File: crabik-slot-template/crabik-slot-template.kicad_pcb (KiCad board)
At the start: 2 copper layers, 50.8 x 50.8 mm, 49 parts, among them J1 Battery, J1 UP (A), J15 CENTER (C) (1), J16 CENTER (D) (1), J17 CENTER (C) (2), J18 CENTER (D) (2), J19 CENTER (C) (3), J2 DOWN (A), J2 QWIIC, J20 CENTER (D) (3), J4 UP (B), J5 DOWN (B), P1 USB-C, SW1 Reset button

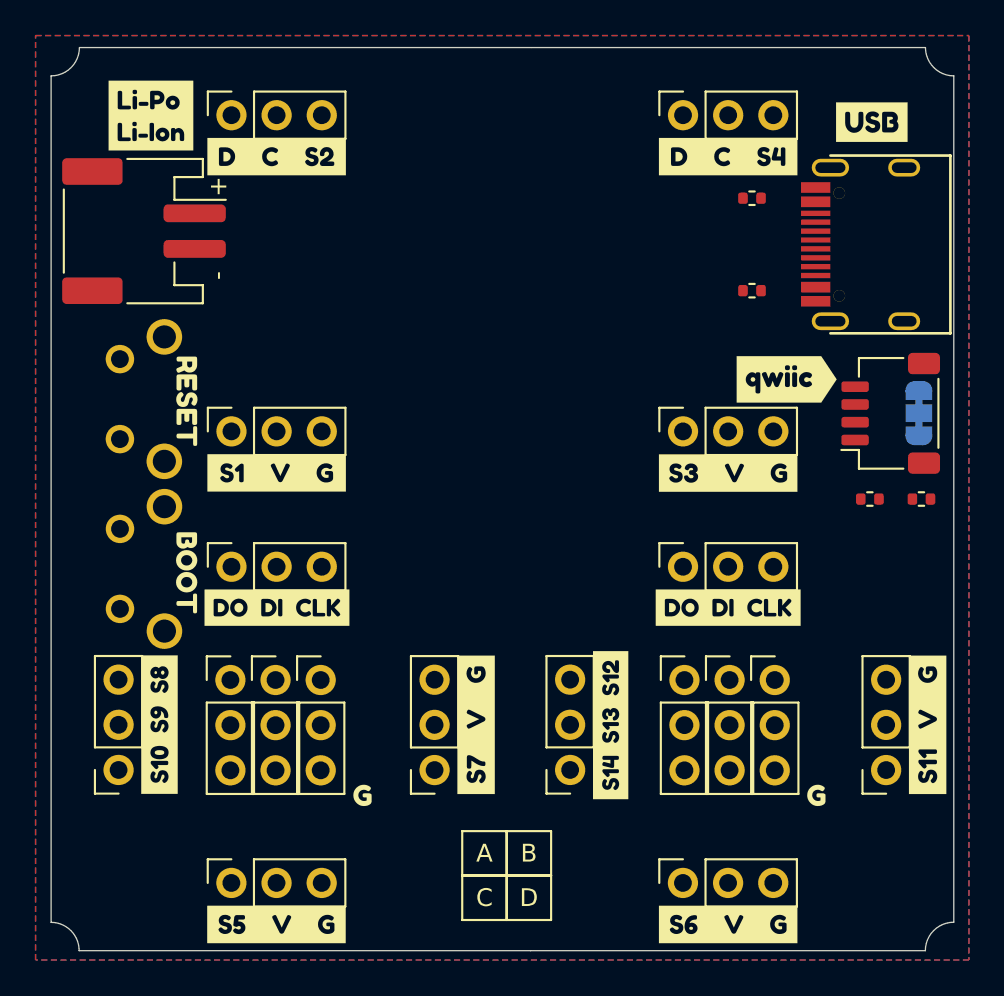
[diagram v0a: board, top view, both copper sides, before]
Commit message: Update templates and CI
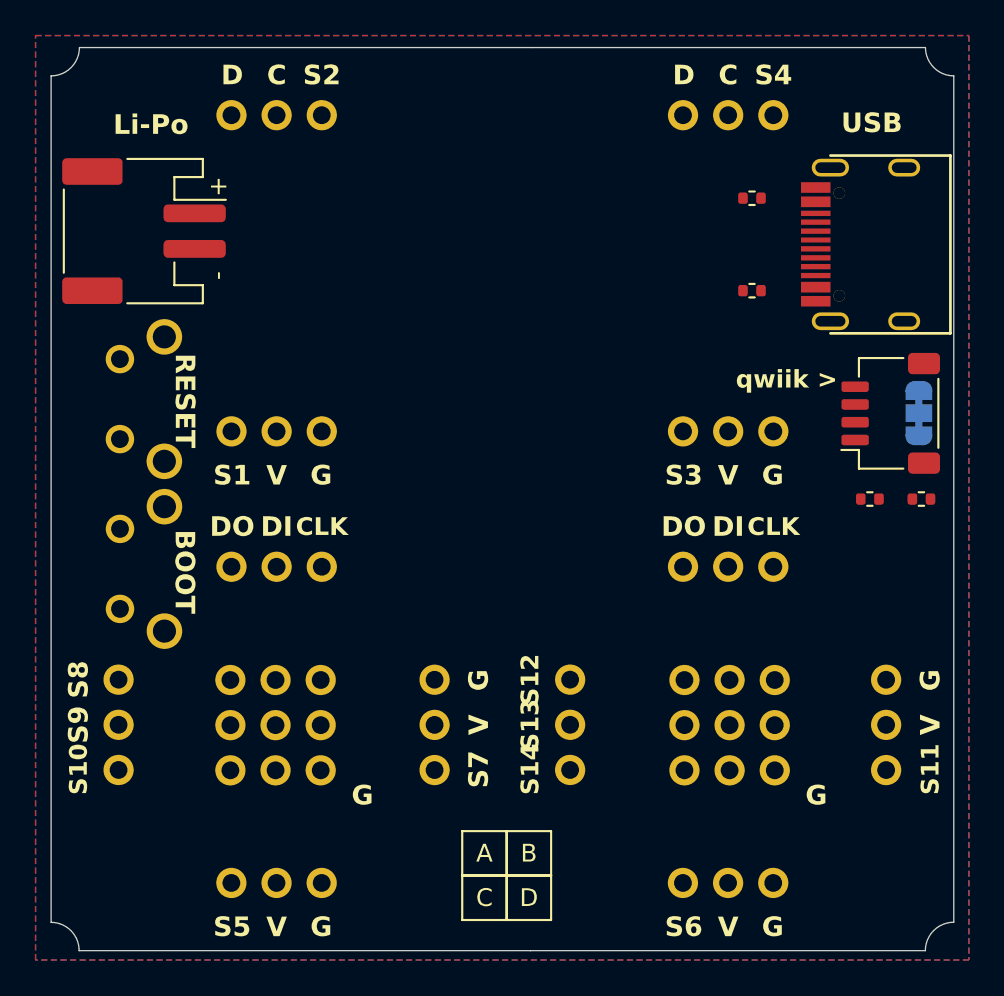
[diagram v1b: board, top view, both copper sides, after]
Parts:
- removed kibuzzard-637F66BD: G***, kibuzzard-637F66BD
- removed kibuzzard-637F7041: G***, kibuzzard-637F7041
- removed kibuzzard-637F708F: G***, kibuzzard-637F708F
- removed kibuzzard-63C28786: G***, kibuzzard-63C28786
- removed kibuzzard-63C28790: G***, kibuzzard-63C28790
- removed kibuzzard-63CA6CBF: G***, kibuzzard-63CA6CBF
- removed kibuzzard-63CE9BA7: G***, kibuzzard-63CE9BA7
- removed kibuzzard-63CFAB43: G***, kibuzzard-63CFAB43
- removed kibuzzard-63CFAB7C: G***, kibuzzard-63CFAB7C
- removed kibuzzard-63CFACF8: G***, kibuzzard-63CFACF8
- removed kibuzzard-63CFADAC: G***, kibuzzard-63CFADAC
- removed kibuzzard-63CFAED5: G***, kibuzzard-63CFAED5
- removed kibuzzard-63CFAF5C: G***, kibuzzard-63CFAF5C
- removed kibuzzard-63CFAFAA: G***, kibuzzard-63CFAFAA
- removed kibuzzard-63CFAFDE: G***, kibuzzard-63CFAFDE
- removed kibuzzard-63CFB14C (x2): G***, kibuzzard-63CFB14C
- removed kibuzzard-63CFB1DC: G***, kibuzzard-63CFB1DC
- removed kibuzzard-63CFB240: G***, kibuzzard-63CFB240
- removed kibuzzard-63CFBBB1 (x2): G***, kibuzzard-63CFBBB1
- renumbered J4 to J10, J5 to J11, J4 to J12, J5 to J13, J1 to J14, J1 to J3, J1 to J4, J2 to J5, J1 to J6, J2 to J7, J1 to J8, J1 to J9, SW1 to SW2
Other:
- board text added: "BOOT"
- board text added: "CLK"
- board text added: "DI"
- board text added: "DO"
- board text added: "G"
- board text added: "Li-Po"
- board text added: "RESET"
- board text added: "S1"
- board text added: "S10"
- board text added: "S11"
- board text added: "S12"
- board text added: "S13"
- board text added: "S14"
- board text added: "S2"
- board text added: "S3"
- board text added: "S4"
- board text added: "S5"
- board text added: "S6"
- board text added: "S7"
- board text added: "S8"
- board text added: "S9"
- board text added: "USB"
- board text added: "V"
- board text added: "qwiik >"
